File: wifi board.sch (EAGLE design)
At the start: 31 parts

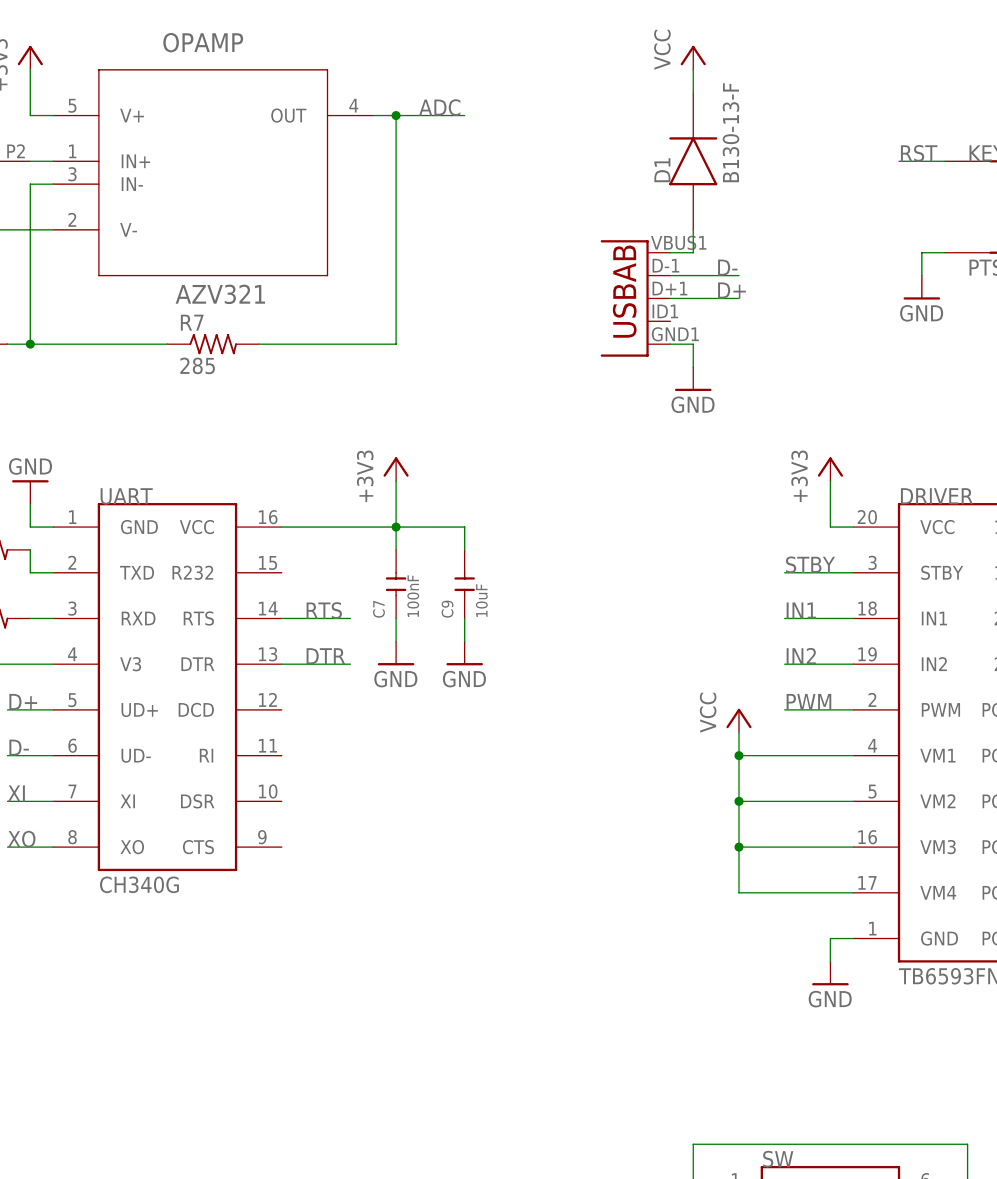
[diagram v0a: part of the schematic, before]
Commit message: finished routing and made gerber files
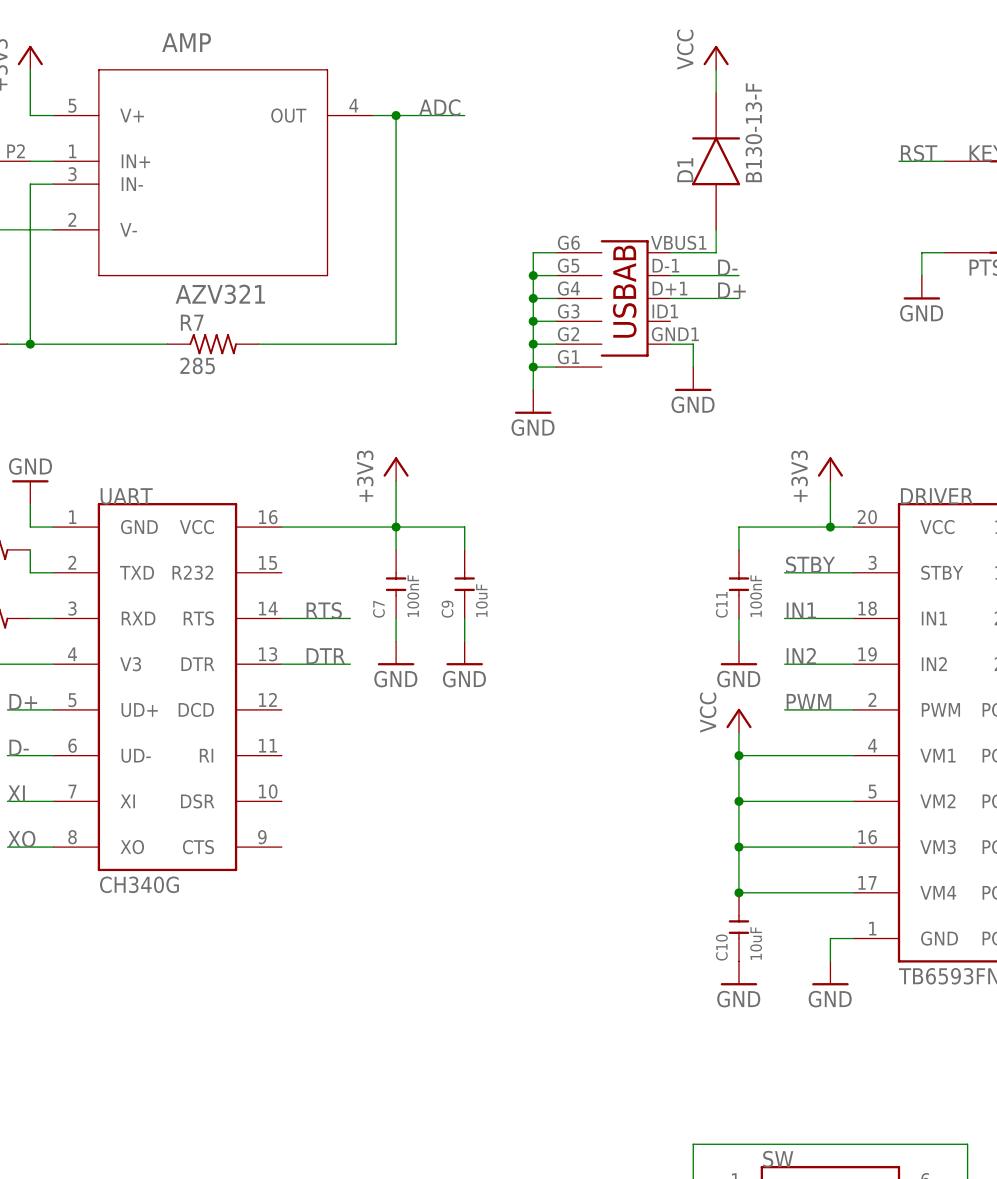
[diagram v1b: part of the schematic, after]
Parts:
- added C10: 10uF, Seeed-OPL-Capacitor:CERAMIC-0.5PF-50V-0.1PF-NPO(0603)
- added C11: 100nF, Seeed-OPL-Capacitor:CERAMIC-0.5PF-50V-0.1PF-NPO(0603)
- renumbered MDL1 to ESP12, OPAMP to AMP, U1 to USB
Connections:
- net N$4 renamed SW
- net +3V3: now also C11.2
- net GND: now also C10.1, C11.1, USB.G1, USB.G2, USB.G3, USB.G4, USB.G5, USB.G6
- net VCC: now also C10.2
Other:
- moved on the sheet: D1

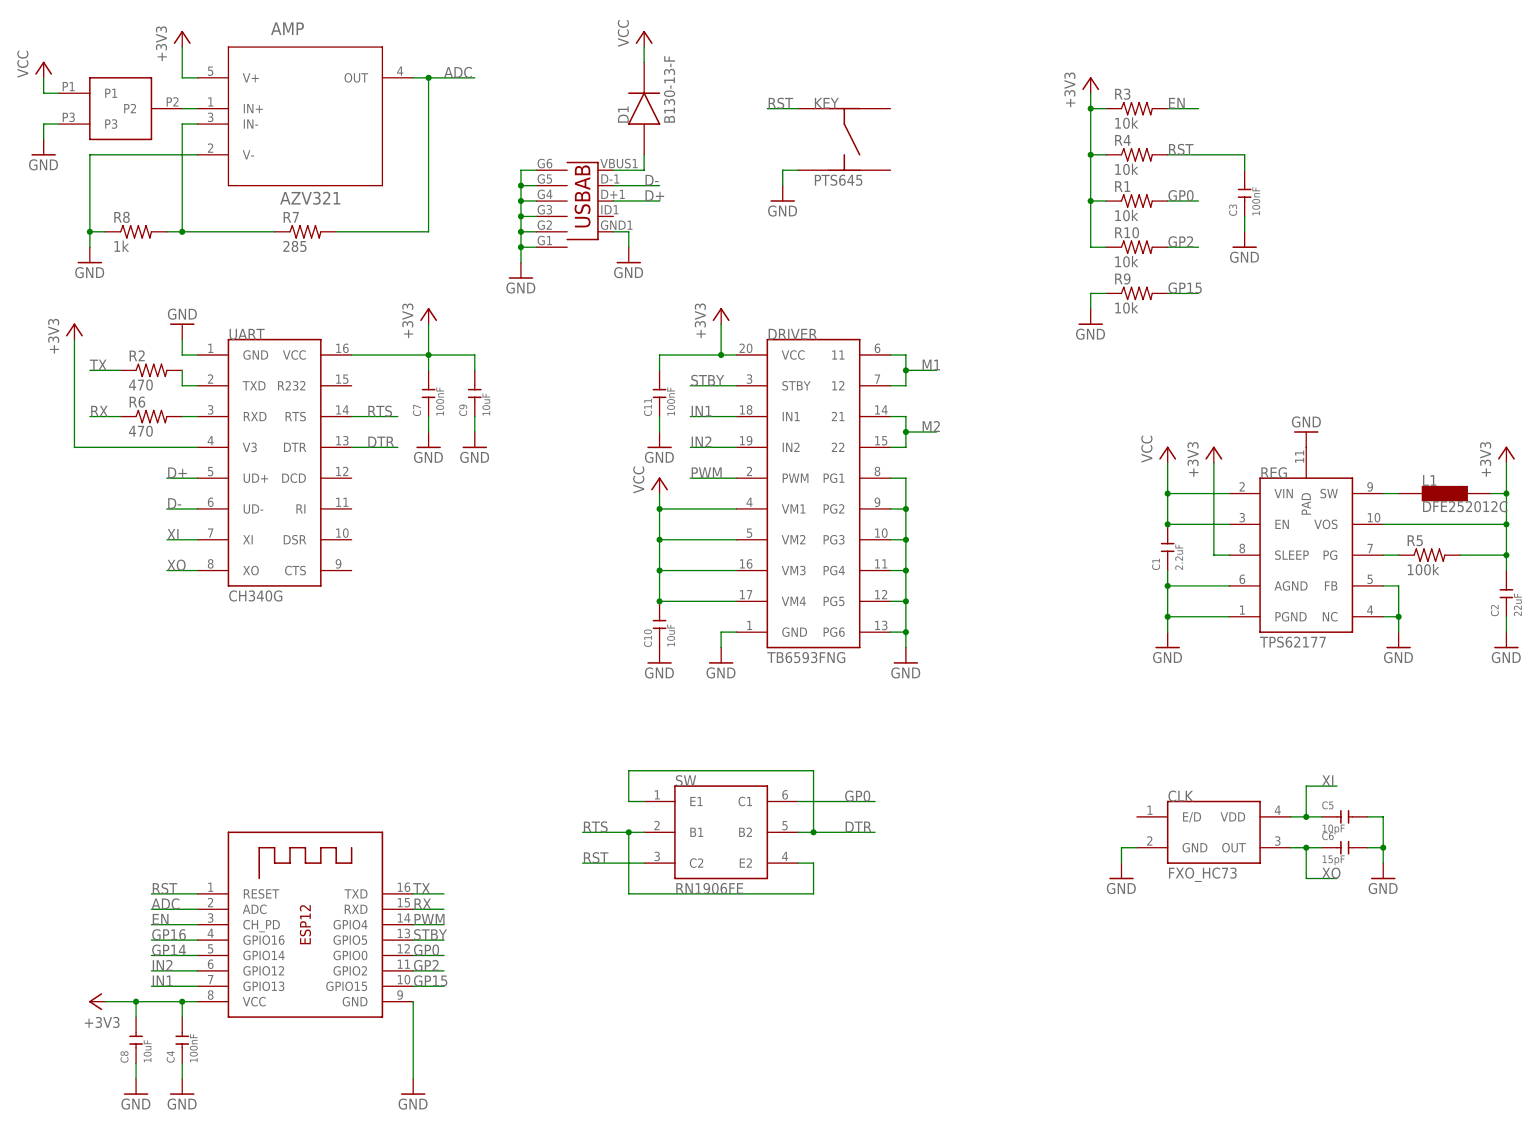
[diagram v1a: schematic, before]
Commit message: added logo, optimized ground pours
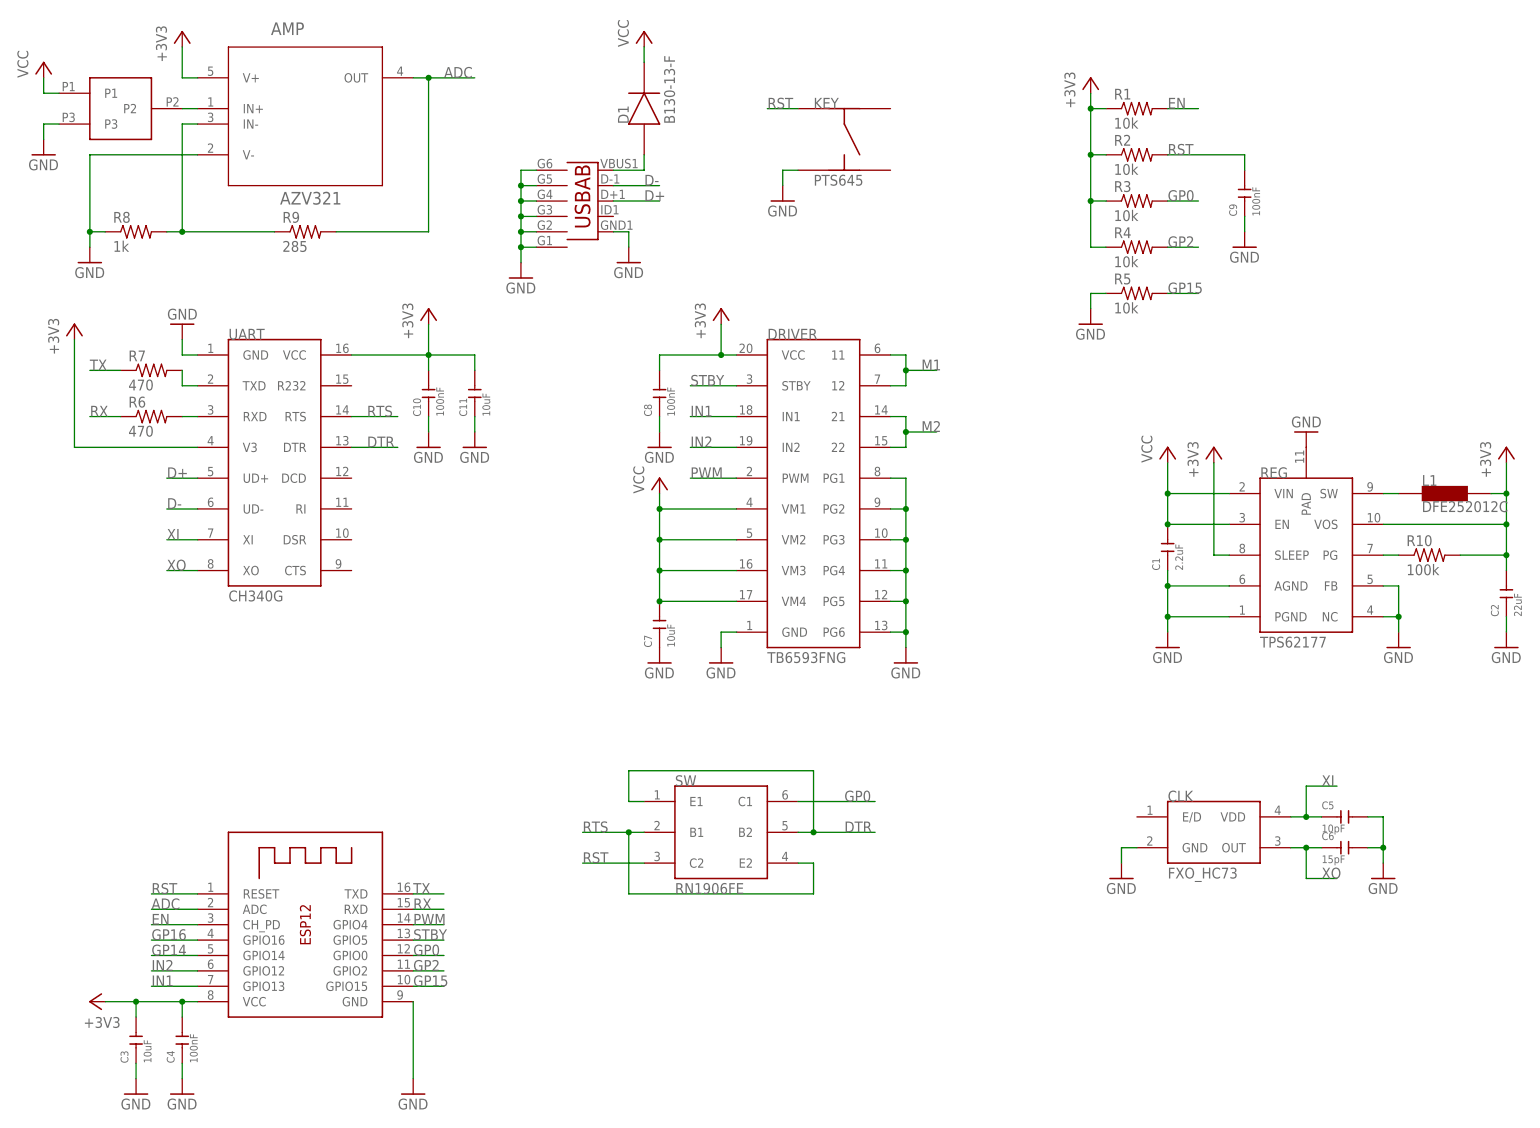
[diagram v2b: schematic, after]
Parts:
- C10, C8: value 10uF -> 100nF
- C11, C7: value 100nF -> 10uF
- C3: value 100nF -> 10uF; device Seeed-OPL-Capacitor:CERAMIC-1PF-50V-0.25PF-NPO(0603) -> Seeed-OPL-Capacitor:CERAMIC-0.5PF-50V-0.1PF-NPO(0603)
- C9: value 10uF -> 100nF; device Seeed-OPL-Capacitor:CERAMIC-0.5PF-50V-0.1PF-NPO(0603) -> Seeed-OPL-Capacitor:CERAMIC-1PF-50V-0.25PF-NPO(0603)
- R10: value 10k -> 100k
- R2: value 470 -> 10k
- R5: value 100k -> 10k
- R7: value 285 -> 470
- R9: value 10k -> 285
- renumbered U$1 to CONN
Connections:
- net +3V3: now also C10.2, C3.2, R10.2, R2.1; no longer C7.2, C9.2, R10.1, R5.2
- net ADC: now also R9.2; no longer R7.2
- net EN: now also R1.2; no longer R3.2
- net GND: now also R5.1; no longer R9.1
- net GP0: now also R3.2; no longer R1.2
- net GP15: now also R5.2; no longer R9.2
- net GP2: now also R4.2; no longer R10.2
- net N$1: now also R7.2; no longer R2.2
- net N$2: now also R10.1; no longer R5.1
- net N$6: now also R9.1; no longer R7.1
- net RST: now also C9.2, R2.2; no longer C3.2, R4.2
- net TX: now also R7.1; no longer R2.1
- net VCC: now also C7.2; no longer C10.2
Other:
- moved on the sheet: C10, C11, C3, C7, C8, C9, R1, R10, R2, R3, R4, R5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
